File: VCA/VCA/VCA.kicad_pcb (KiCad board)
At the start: 2 copper layers, 68.1 x 53.3 mm, 70 parts, among them J10 Conn_01x03, J11 Conn_01x03, J12 Conn_01x03, J13 Conn_01x02, J14 Conn_01x03, J15 Conn_01x03, J16 Conn_01x02, J9 Conn_02x05_Odd_Even, Q1 2N3904, Q2 2N3906, Q3 2N3904, Q4 2N3906, U1 TL084, U2 LM13700

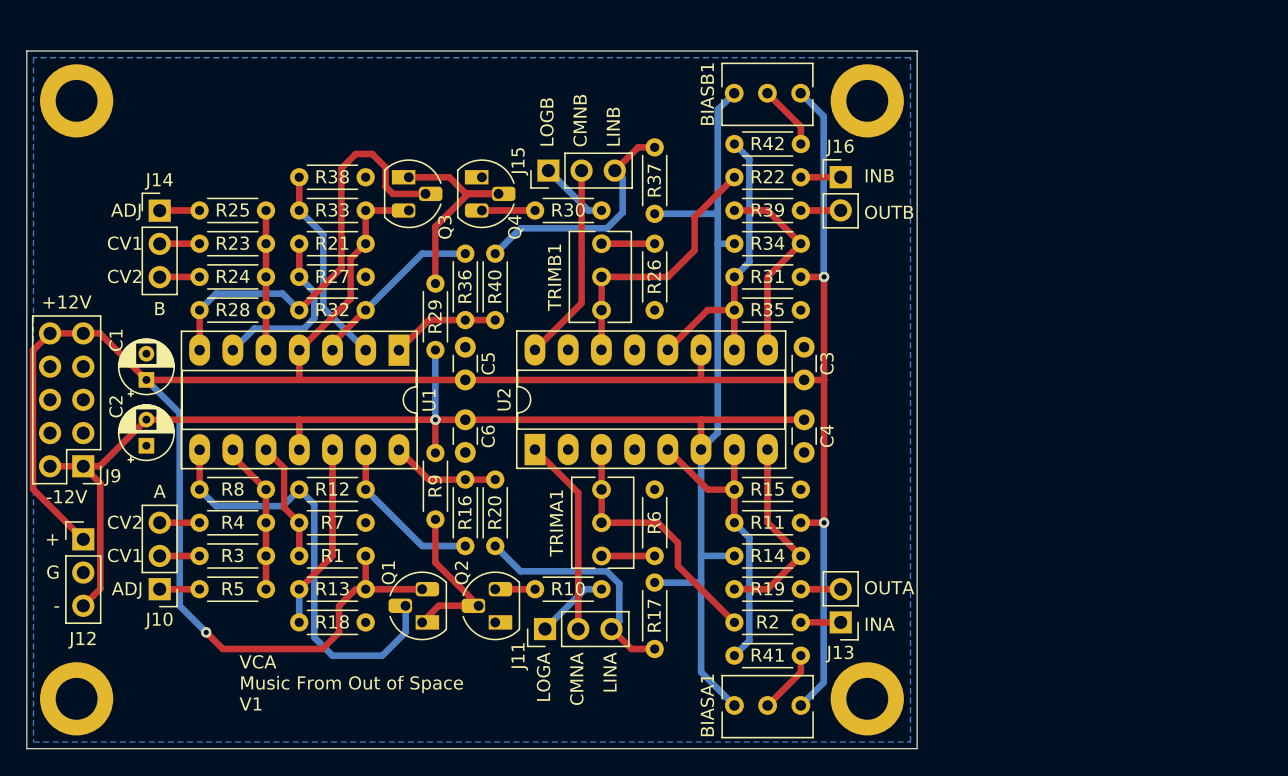
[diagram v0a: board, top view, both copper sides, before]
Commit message: VCA - correct resistors sizes
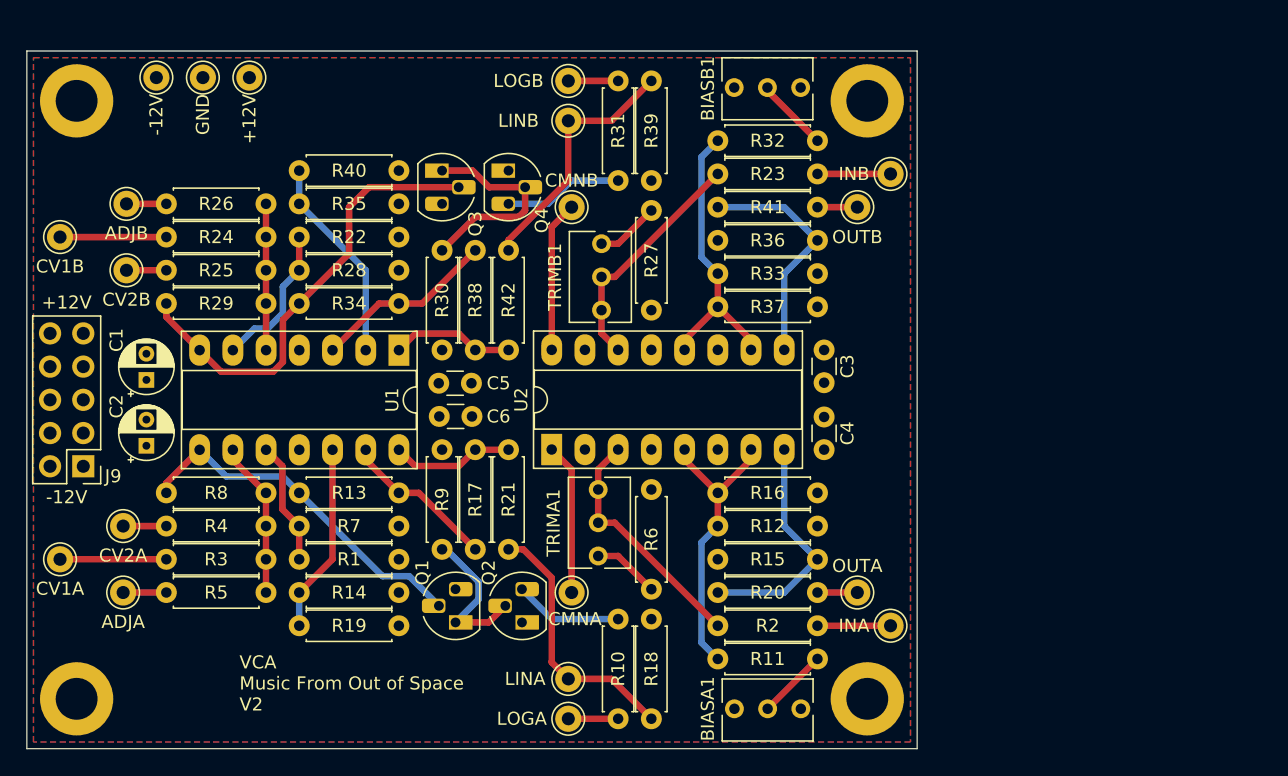
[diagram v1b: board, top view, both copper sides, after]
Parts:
- removed J10, J11, J12, J14, J15: Conn_01x03, Connector_PinHeader_2.54mm:PinHeader_1x03_P2.54mm_Vertical
- removed J13, J16: Conn_01x02, Connector_PinHeader_2.54mm:PinHeader_1x02_P2.54mm_Vertical
- added +12V: Conn_01x01_Pin, Connector_Pin:Pin_D1.0mm_L10.0mm, F.Cu at (89.4, 28.7)
- added -12V: Conn_01x01_Pin, Connector_Pin:Pin_D1.0mm_L10.0mm, F.Cu at (82.3, 28.7)
- added ADJA: Conn_01x01_Pin, Connector_Pin:Pin_D1.0mm_L10.0mm, F.Cu at (79.8, 68.1)
- added ADJB: Conn_01x01_Pin, Connector_Pin:Pin_D1.0mm_L10.0mm, F.Cu at (80.0, 38.4)
- added CMNA: Conn_01x01_Pin, Connector_Pin:Pin_D1.0mm_L10.0mm, F.Cu at (114.0, 68.1)
- added CMNB: Conn_01x01_Pin, Connector_Pin:Pin_D1.0mm_L10.0mm, F.Cu at (114.0, 38.6)
- added CV1A: Conn_01x01_Pin, Connector_Pin:Pin_D1.0mm_L10.0mm, F.Cu at (74.9, 65.5)
- added CV1B: Conn_01x01_Pin, Connector_Pin:Pin_D1.0mm_L10.0mm, F.Cu at (74.9, 40.9)
- added CV2A: Conn_01x01_Pin, Connector_Pin:Pin_D1.0mm_L10.0mm, F.Cu at (79.8, 63.0)
- added CV2B: Conn_01x01_Pin, Connector_Pin:Pin_D1.0mm_L10.0mm, F.Cu at (80.0, 43.4)
- added GND: Conn_01x01_Pin, Connector_Pin:Pin_D1.0mm_L10.0mm, F.Cu at (85.9, 28.7)
- added INA: Conn_01x01_Pin, Connector_Pin:Pin_D1.0mm_L10.0mm, F.Cu at (138.4, 70.6)
- added INB: Conn_01x01_Pin, Connector_Pin:Pin_D1.0mm_L10.0mm, F.Cu at (138.4, 36.1)
- added LINA: Conn_01x01_Pin, Connector_Pin:Pin_D1.0mm_L10.0mm, F.Cu at (113.8, 74.7)
- added LINB: Conn_01x01_Pin, Connector_Pin:Pin_D1.0mm_L10.0mm, F.Cu at (113.8, 32.0)
- added LOGA: Conn_01x01_Pin, Connector_Pin:Pin_D1.0mm_L10.0mm, F.Cu at (113.8, 77.7)
- added LOGB: Conn_01x01_Pin, Connector_Pin:Pin_D1.0mm_L10.0mm, F.Cu at (113.8, 29.0)
- added OUTA: Conn_01x01_Pin, Connector_Pin:Pin_D1.0mm_L10.0mm, F.Cu at (135.9, 68.1)
- added OUTB: Conn_01x01_Pin, Connector_Pin:Pin_D1.0mm_L10.0mm, F.Cu at (135.9, 38.6)
- R1, R10, R2, R3, R4, R5, R6, R7, R8, R9: footprint Resistor_THT:R_Axial_DIN0204_L3.6mm_D1.6mm_P5.08mm_Horizontal -> Library:R_Axial_DIN0207_L6.3mm_D2.5mm_P7.62mm_Horizontal
- R11: renamed from R41; footprint Resistor_THT:R_Axial_DIN0204_L3.6mm_D1.6mm_P5.08mm_Horizontal -> Library:R_Axial_DIN0207_L6.3mm_D2.5mm_P7.62mm_Horizontal
- R12: renamed from R11; footprint Resistor_THT:R_Axial_DIN0204_L3.6mm_D1.6mm_P5.08mm_Horizontal -> Library:R_Axial_DIN0207_L6.3mm_D2.5mm_P7.62mm_Horizontal
- R13: renamed from R12; footprint Resistor_THT:R_Axial_DIN0204_L3.6mm_D1.6mm_P5.08mm_Horizontal -> Library:R_Axial_DIN0207_L6.3mm_D2.5mm_P7.62mm_Horizontal
- R14: renamed from R13; footprint Resistor_THT:R_Axial_DIN0204_L3.6mm_D1.6mm_P5.08mm_Horizontal -> Library:R_Axial_DIN0207_L6.3mm_D2.5mm_P7.62mm_Horizontal
- R15: renamed from R14; footprint Resistor_THT:R_Axial_DIN0204_L3.6mm_D1.6mm_P5.08mm_Horizontal -> Library:R_Axial_DIN0207_L6.3mm_D2.5mm_P7.62mm_Horizontal
- R16: renamed from R15; footprint Resistor_THT:R_Axial_DIN0204_L3.6mm_D1.6mm_P5.08mm_Horizontal -> Library:R_Axial_DIN0207_L6.3mm_D2.5mm_P7.62mm_Horizontal
- R17: renamed from R16; footprint Resistor_THT:R_Axial_DIN0204_L3.6mm_D1.6mm_P5.08mm_Horizontal -> Library:R_Axial_DIN0207_L6.3mm_D2.5mm_P7.62mm_Horizontal
- R18: renamed from R17; footprint Resistor_THT:R_Axial_DIN0204_L3.6mm_D1.6mm_P5.08mm_Horizontal -> Library:R_Axial_DIN0207_L6.3mm_D2.5mm_P7.62mm_Horizontal
- R19: renamed from R18; footprint Resistor_THT:R_Axial_DIN0204_L3.6mm_D1.6mm_P5.08mm_Horizontal -> Library:R_Axial_DIN0207_L6.3mm_D2.5mm_P7.62mm_Horizontal
- R20: renamed from R19; footprint Resistor_THT:R_Axial_DIN0204_L3.6mm_D1.6mm_P5.08mm_Horizontal -> Library:R_Axial_DIN0207_L6.3mm_D2.5mm_P7.62mm_Horizontal
- R21: renamed from R20; footprint Resistor_THT:R_Axial_DIN0204_L3.6mm_D1.6mm_P5.08mm_Horizontal -> Library:R_Axial_DIN0207_L6.3mm_D2.5mm_P7.62mm_Horizontal
- R22: renamed from R21; footprint Resistor_THT:R_Axial_DIN0204_L3.6mm_D1.6mm_P5.08mm_Horizontal -> Library:R_Axial_DIN0207_L6.3mm_D2.5mm_P7.62mm_Horizontal
- R23: renamed from R22; footprint Resistor_THT:R_Axial_DIN0204_L3.6mm_D1.6mm_P5.08mm_Horizontal -> Library:R_Axial_DIN0207_L6.3mm_D2.5mm_P7.62mm_Horizontal
- R24: renamed from R23; footprint Resistor_THT:R_Axial_DIN0204_L3.6mm_D1.6mm_P5.08mm_Horizontal -> Library:R_Axial_DIN0207_L6.3mm_D2.5mm_P7.62mm_Horizontal
- R25: renamed from R24; footprint Resistor_THT:R_Axial_DIN0204_L3.6mm_D1.6mm_P5.08mm_Horizontal -> Library:R_Axial_DIN0207_L6.3mm_D2.5mm_P7.62mm_Horizontal
- R26: renamed from R25; footprint Resistor_THT:R_Axial_DIN0204_L3.6mm_D1.6mm_P5.08mm_Horizontal -> Library:R_Axial_DIN0207_L6.3mm_D2.5mm_P7.62mm_Horizontal
- R27: renamed from R26; footprint Resistor_THT:R_Axial_DIN0204_L3.6mm_D1.6mm_P5.08mm_Horizontal -> Library:R_Axial_DIN0207_L6.3mm_D2.5mm_P7.62mm_Horizontal
- R28: renamed from R27; footprint Resistor_THT:R_Axial_DIN0204_L3.6mm_D1.6mm_P5.08mm_Horizontal -> Library:R_Axial_DIN0207_L6.3mm_D2.5mm_P7.62mm_Horizontal
- R29: renamed from R28; footprint Resistor_THT:R_Axial_DIN0204_L3.6mm_D1.6mm_P5.08mm_Horizontal -> Library:R_Axial_DIN0207_L6.3mm_D2.5mm_P7.62mm_Horizontal
- R30: renamed from R29; footprint Resistor_THT:R_Axial_DIN0204_L3.6mm_D1.6mm_P5.08mm_Horizontal -> Library:R_Axial_DIN0207_L6.3mm_D2.5mm_P7.62mm_Horizontal
- R31: renamed from R30; footprint Resistor_THT:R_Axial_DIN0204_L3.6mm_D1.6mm_P5.08mm_Horizontal -> Library:R_Axial_DIN0207_L6.3mm_D2.5mm_P7.62mm_Horizontal
- R32: renamed from R42; footprint Resistor_THT:R_Axial_DIN0204_L3.6mm_D1.6mm_P5.08mm_Horizontal -> Library:R_Axial_DIN0207_L6.3mm_D2.5mm_P7.62mm_Horizontal
- R33: renamed from R31; footprint Resistor_THT:R_Axial_DIN0204_L3.6mm_D1.6mm_P5.08mm_Horizontal -> Library:R_Axial_DIN0207_L6.3mm_D2.5mm_P7.62mm_Horizontal
- R34: renamed from R32; footprint Resistor_THT:R_Axial_DIN0204_L3.6mm_D1.6mm_P5.08mm_Horizontal -> Library:R_Axial_DIN0207_L6.3mm_D2.5mm_P7.62mm_Horizontal
- R35: renamed from R33; footprint Resistor_THT:R_Axial_DIN0204_L3.6mm_D1.6mm_P5.08mm_Horizontal -> Library:R_Axial_DIN0207_L6.3mm_D2.5mm_P7.62mm_Horizontal
- R36: renamed from R34; footprint Resistor_THT:R_Axial_DIN0204_L3.6mm_D1.6mm_P5.08mm_Horizontal -> Library:R_Axial_DIN0207_L6.3mm_D2.5mm_P7.62mm_Horizontal
- R37: renamed from R35; footprint Resistor_THT:R_Axial_DIN0204_L3.6mm_D1.6mm_P5.08mm_Horizontal -> Library:R_Axial_DIN0207_L6.3mm_D2.5mm_P7.62mm_Horizontal
- R38: renamed from R36; footprint Resistor_THT:R_Axial_DIN0204_L3.6mm_D1.6mm_P5.08mm_Horizontal -> Library:R_Axial_DIN0207_L6.3mm_D2.5mm_P7.62mm_Horizontal
- R39: renamed from R37; footprint Resistor_THT:R_Axial_DIN0204_L3.6mm_D1.6mm_P5.08mm_Horizontal -> Library:R_Axial_DIN0207_L6.3mm_D2.5mm_P7.62mm_Horizontal
- R40: renamed from R38; footprint Resistor_THT:R_Axial_DIN0204_L3.6mm_D1.6mm_P5.08mm_Horizontal -> Library:R_Axial_DIN0207_L6.3mm_D2.5mm_P7.62mm_Horizontal
- R41: renamed from R39; footprint Resistor_THT:R_Axial_DIN0204_L3.6mm_D1.6mm_P5.08mm_Horizontal -> Library:R_Axial_DIN0207_L6.3mm_D2.5mm_P7.62mm_Horizontal
- R42: renamed from R40; footprint Resistor_THT:R_Axial_DIN0204_L3.6mm_D1.6mm_P5.08mm_Horizontal -> Library:R_Axial_DIN0207_L6.3mm_D2.5mm_P7.62mm_Horizontal
- moved R10 9.99 mm to (117.6, 77.7), turned to 90 degrees
- moved R31 9.99 mm to (117.6, 29.0), turned to -90 degrees
- moved R18 2.81 mm to (120.1, 70.1)
- moved C6 2.80 mm to (106.4, 54.6), turned to 180 degrees
- moved Q3 2.59 mm to (104.1, 35.8)
- moved R22 2.59 mm to (100.8, 40.9)
- moved R24 2.59 mm to (83.1, 40.9)
- moved R25 2.59 mm to (83.1, 43.4)
- moved R26 2.59 mm to (83.1, 38.4)
- moved R35 2.59 mm to (100.8, 38.4)
- moved R39 2.55 mm to (120.1, 36.6)
- moved R14 2.55 mm to (100.8, 68.1)
- moved R5 2.55 mm to (83.1, 68.1)
- moved R4 2.55 mm to (83.1, 63.0)
- moved R1 2.55 mm to (100.8, 65.5)
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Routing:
- net +12V: track 194.9 -> 0.00 mm, vias 3 -> 0
- net -12V: track 144.4 -> 0.00 mm, vias 1 -> 0
- net Net-(Q1-B): track 33.8 -> 27.9 mm
- net Net-(Q2-C): track 3.05 -> 8.30 mm
- net CV1A: track 3.05 -> 8.13 mm
- net CV1B: track 3.05 -> 8.13 mm
- net Net-(Q4-C): track 4.06 -> 9.12 mm
- net CMNB: track 15.2 -> 11.5 mm
- net CMNA: track 15.1 -> 11.6 mm
- net Net-(R15-Pad2): track 15.3 -> 18.1 mm
- net Net-(R36-Pad2): track 15.3 -> 18.1 mm
- net INA: track 3.05 -> 5.59 mm
- net INB: track 3.05 -> 5.59 mm
- net Net-(U2A-+): track 20.4 -> 18.3 mm
- net Net-(U1B--): track 13.4 -> 11.3 mm
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- added copper zone on F.Cu, net +12V
- added copper zone on B.Cu, net -12V
- added copper zone on In1.Cu, net GND
- added copper zone on In2.Cu, net GND
- removed copper zone on B.Cu, net GND
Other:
- copper layers 2 -> 4
- board text added: "VCA Music From Out of Space V2"
- board text removed: "+"
- board text removed: "-"
- board text removed: "A"
- board text removed: "ADJ"
- board text removed: "B"
- board text removed: "CMNA"
- board text removed: "CMNB"
- board text removed: "CV1"
- board text removed: "CV2"
- board text removed: "G"
- board text removed: "INA"
- board text removed: "INB"
- board text removed: "LINA"
- board text removed: "LINB"
- board text removed: "LOGA"
- board text removed: "LOGB"
- board text removed: "OUTA"
- board text removed: "OUTB"
- board text removed: "VCA Music From Out of Space V1"

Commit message: VCA - updated trim pot footprint, partial fix
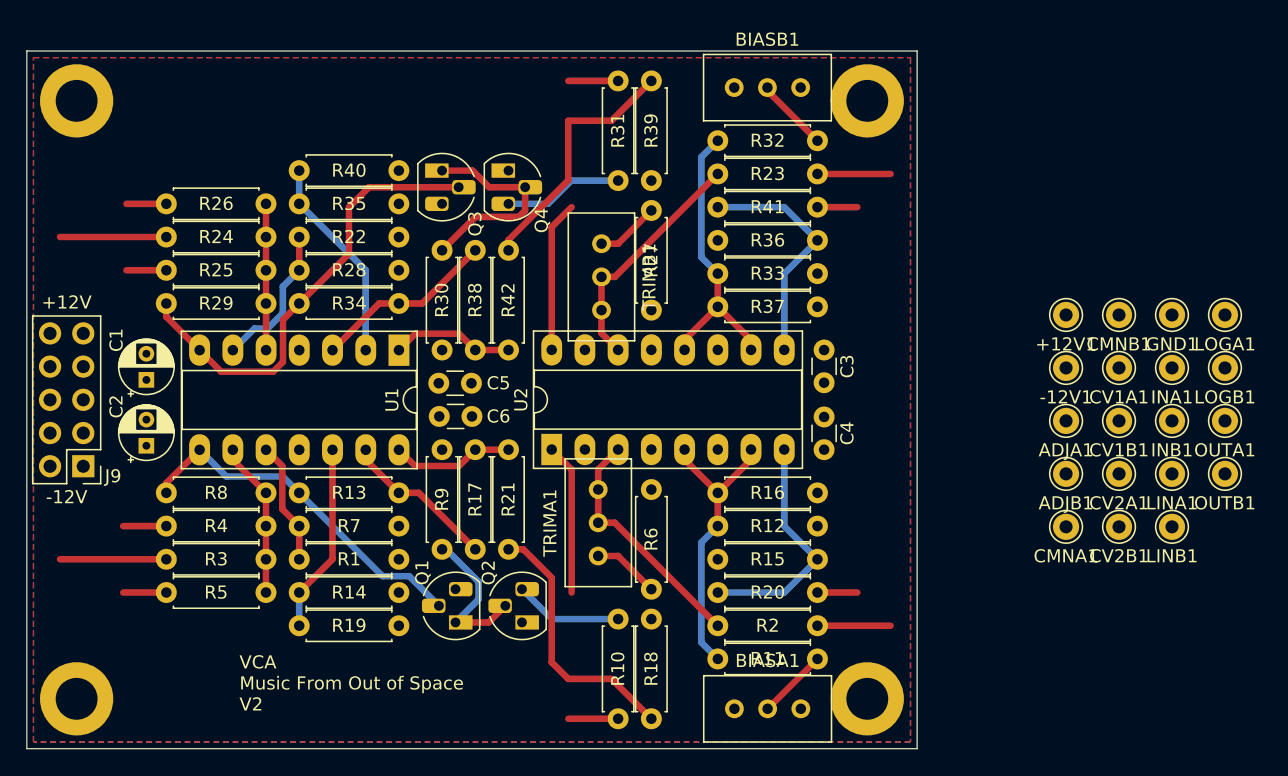
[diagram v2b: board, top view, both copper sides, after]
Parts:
- removed +12V, -12V, ADJA, ADJB, CMNA, CMNB, CV1A, CV1B, CV2A, CV2B, GND, INA, INB, LINA, LINB, LOGA, LOGB, OUTA, OUTB: Conn_01x01_Pin, Connector_Pin:Pin_D1.0mm_L10.0mm
- added +12V1: Conn_01x01_Pin, Connector_Pin:Pin_D1.0mm_L10.0mm, F.Cu at (151.8, 46.9)
- added -12V1: Conn_01x01_Pin, Connector_Pin:Pin_D1.0mm_L10.0mm, F.Cu at (151.8, 50.9)
- added ADJA1: Conn_01x01_Pin, Connector_Pin:Pin_D1.0mm_L10.0mm, F.Cu at (151.8, 55.0)
- added ADJB1: Conn_01x01_Pin, Connector_Pin:Pin_D1.0mm_L10.0mm, F.Cu at (151.8, 59.0)
- added CMNA1: Conn_01x01_Pin, Connector_Pin:Pin_D1.0mm_L10.0mm, F.Cu at (151.8, 63.0)
- added CMNB1: Conn_01x01_Pin, Connector_Pin:Pin_D1.0mm_L10.0mm, F.Cu at (155.9, 46.9)
- added CV1A1: Conn_01x01_Pin, Connector_Pin:Pin_D1.0mm_L10.0mm, F.Cu at (155.9, 50.9)
- added CV1B1: Conn_01x01_Pin, Connector_Pin:Pin_D1.0mm_L10.0mm, F.Cu at (155.9, 55.0)
- added CV2A1: Conn_01x01_Pin, Connector_Pin:Pin_D1.0mm_L10.0mm, F.Cu at (155.9, 59.0)
- added CV2B1: Conn_01x01_Pin, Connector_Pin:Pin_D1.0mm_L10.0mm, F.Cu at (155.9, 63.0)
- added GND1: Conn_01x01_Pin, Connector_Pin:Pin_D1.0mm_L10.0mm, F.Cu at (159.9, 46.9)
- added INA1: Conn_01x01_Pin, Connector_Pin:Pin_D1.0mm_L10.0mm, F.Cu at (159.9, 50.9)
- added INB1: Conn_01x01_Pin, Connector_Pin:Pin_D1.0mm_L10.0mm, F.Cu at (159.9, 55.0)
- added LINA1: Conn_01x01_Pin, Connector_Pin:Pin_D1.0mm_L10.0mm, F.Cu at (159.9, 59.0)
- added LINB1: Conn_01x01_Pin, Connector_Pin:Pin_D1.0mm_L10.0mm, F.Cu at (159.9, 63.0)
- added LOGA1: Conn_01x01_Pin, Connector_Pin:Pin_D1.0mm_L10.0mm, F.Cu at (164.0, 46.9)
- added LOGB1: Conn_01x01_Pin, Connector_Pin:Pin_D1.0mm_L10.0mm, F.Cu at (164.0, 50.9)
- added OUTA1: Conn_01x01_Pin, Connector_Pin:Pin_D1.0mm_L10.0mm, F.Cu at (164.0, 55.0)
- added OUTB1: Conn_01x01_Pin, Connector_Pin:Pin_D1.0mm_L10.0mm, F.Cu at (164.0, 59.0)
- BIASA1, BIASB1, TRIMA1, TRIMB1: footprint Potentiometer_THT:Potentiometer_Bourns_3266Y_Vertical -> Potentiometer_THT:Potentiometer_Bourns_3296W_Vertical
